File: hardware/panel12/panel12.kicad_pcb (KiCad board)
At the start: 2 copper layers, 99 x 92 mm, 300 parts, among them J1 Conn_01x02_Male, J2 Conn_01x08_Male, J3 Conn_01x02, J5 Conn_01x02_Male, J6 Conn_01x02_Male, J7 Conn_01x02_Male, U1 A7105-MODULE, U2 AIC1734-33GUTR, U3 ATtiny1617-M, U5 DRV8837DSGR, U6 DRV8837DSGR, U7 DRV8837DSGR

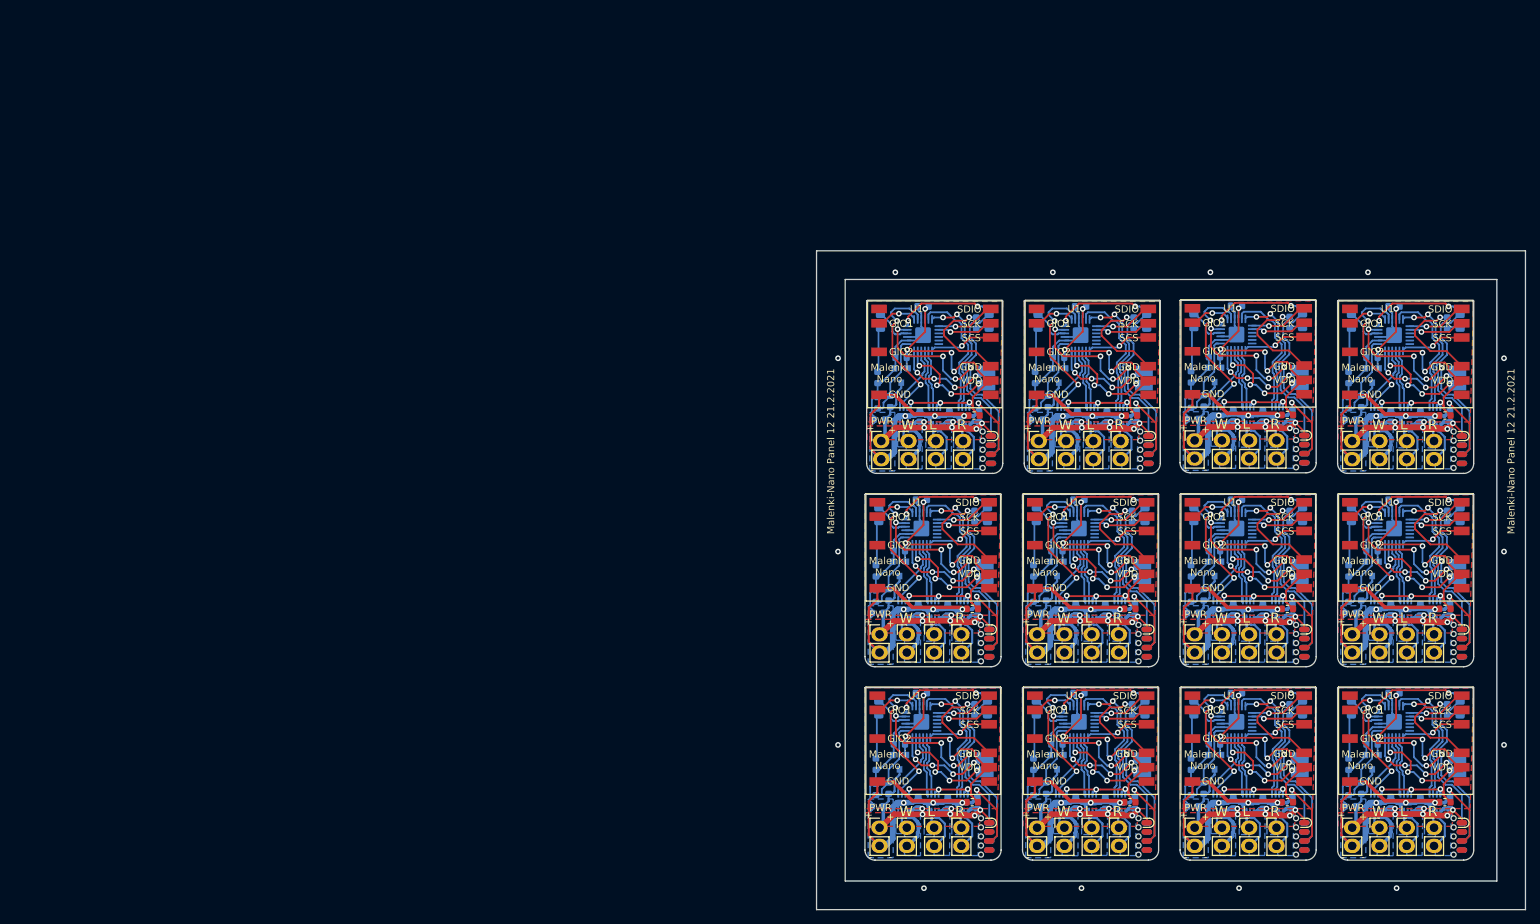
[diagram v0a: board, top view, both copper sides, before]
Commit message: Panel of 12 boards with the changes for tiny817
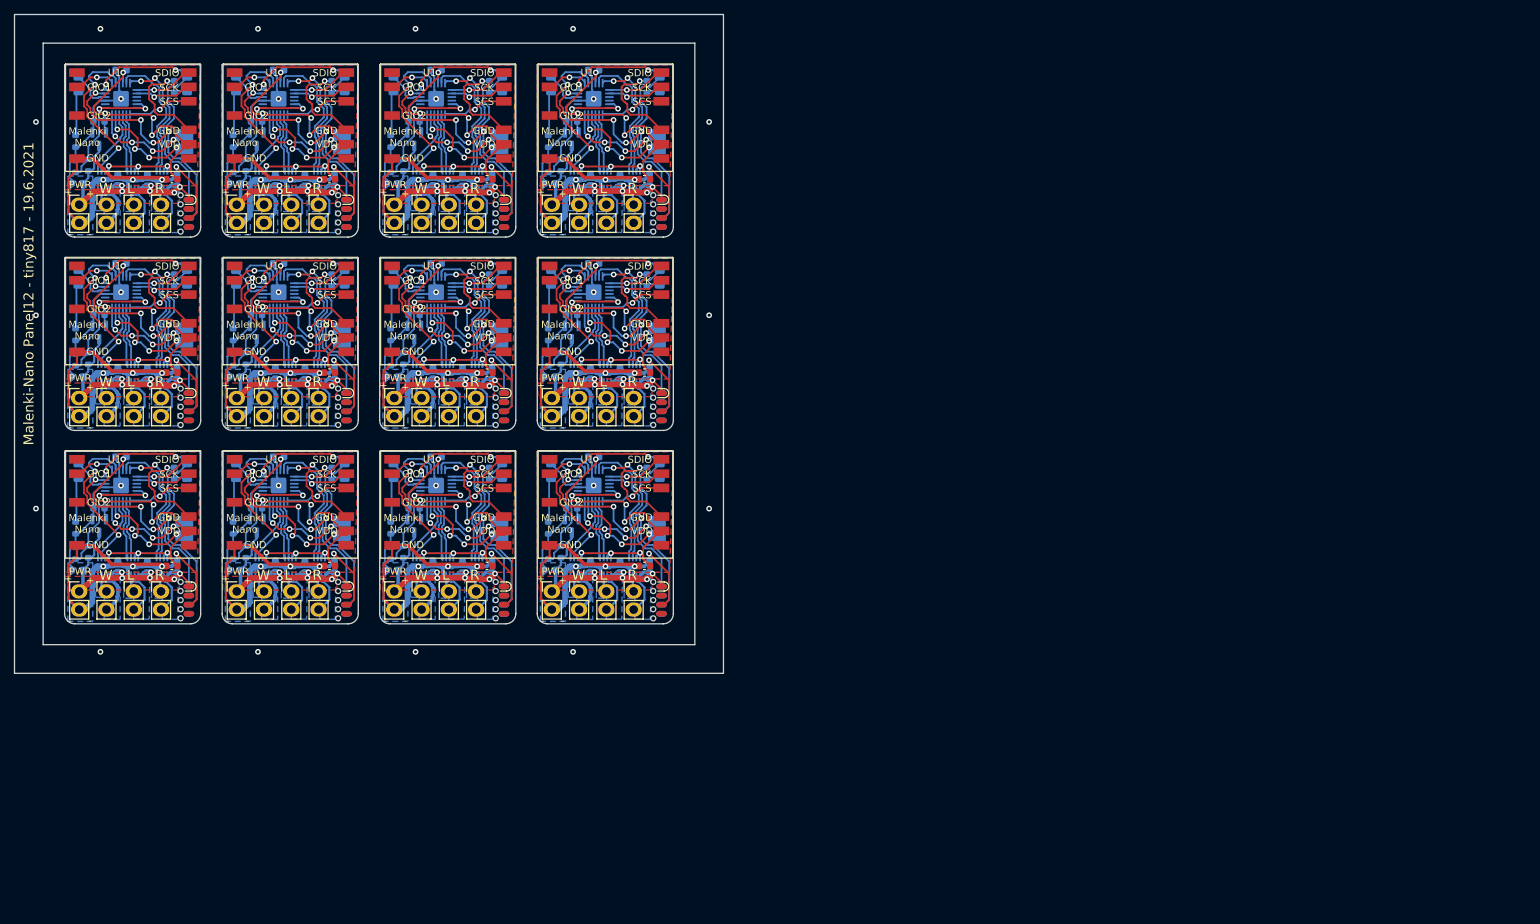
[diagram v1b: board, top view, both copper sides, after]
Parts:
- removed the C1 at (172.0, 96.0)
- removed the C1 at (193.8, 150.0)
- removed the C1 at (215.8, 150.0)
- removed the C1 at (215.8, 123.0)
- removed the C1 at (171.8, 123.0)
- removed the C1 at (171.8, 150.0)
- removed the C1 at (150.0, 96.0)
- removed the C1 at (193.8, 95.9)
- removed the C1 at (149.8, 150.0)
- removed the C1 at (193.8, 123.0)
- removed the C1 at (215.8, 96.0)
- removed the C1 at (149.8, 123.0)
- removed the C2 at (180.5, 123.6)
- removed the C2 at (202.5, 150.6)
- removed the C2 at (158.5, 150.6)
- removed the C2 at (180.5, 96.5)
- removed the C2 at (180.5, 150.6)
- removed the C2 at (202.5, 96.6)
- removed the C2 at (136.5, 150.6)
- removed the C2 at (158.8, 96.6)
- removed the C2 at (158.5, 123.6)
- removed the C2 at (136.8, 96.6)
- removed the C2 at (202.5, 123.6)
- removed the C2 at (136.5, 123.6)
- removed the C3 at (183.6, 114.9)
- removed the C3 at (205.6, 114.9)
- removed the C3 at (205.6, 87.9)
- removed the C3 at (139.8, 87.9)
- removed the C3 at (139.6, 114.9)
- removed the C3 at (161.6, 114.9)
- removed the C3 at (183.6, 87.8)
- removed the C3 at (205.6, 141.9)
- removed the C3 at (139.6, 141.9)
- removed the C3 at (183.6, 141.9)
- removed the C3 at (161.8, 87.9)
- removed the C3 at (161.6, 141.9)
- removed the C4 at (164.9, 80.8)
- removed the C4 at (208.6, 107.8)
- removed the C4 at (208.6, 80.8)
- removed the C4 at (164.6, 134.8)
- removed the C4 at (186.6, 107.8)
- removed the C4 at (142.6, 134.8)
- removed the C4 at (164.6, 107.8)
- removed the C4 at (142.9, 80.8)
- removed the C4 at (186.6, 80.7)
- removed the C4 at (208.6, 134.8)
- removed the C4 at (186.6, 134.8)
- removed the C4 at (142.6, 107.8)
- removed the C5 at (186.2, 96.0)
- removed the C5 at (142.4, 96.1)
- removed the C5 at (186.2, 123.1)
- removed the C5 at (186.2, 150.1)
- removed the C5 at (142.2, 123.1)
- removed the C5 at (208.2, 123.1)
- removed the C5 at (164.2, 150.1)
- removed the C5 at (164.2, 123.1)
- removed the C5 at (142.2, 150.1)
- removed the C5 at (208.2, 150.1)
- removed the C5 at (164.4, 96.1)
- removed the C5 at (208.2, 96.1)
- removed the C6 at (146.3, 150.1)
- removed the C6 at (212.3, 150.1)
- removed the C6 at (212.3, 123.1)
- removed the C6 at (190.3, 150.1)
- removed the C6 at (212.3, 96.1)
- removed the C6 at (190.3, 96.0)
- removed the C6 at (168.3, 123.1)
- removed the C6 at (168.3, 150.1)
- removed the C6 at (146.6, 96.1)
- removed the C6 at (168.6, 96.1)
- removed the C6 at (146.3, 123.1)
- removed the C6 at (190.3, 123.1)
- removed the C7 at (172.7, 96.1)
- removed the C7 at (172.4, 123.1)
- removed the C7 at (172.4, 150.1)
- removed the C7 at (216.4, 96.1)
- removed the C7 at (150.4, 123.1)
- removed the C7 at (216.4, 150.1)
- removed the C7 at (194.4, 96.0)
- removed the C7 at (150.7, 96.1)
- removed the C7 at (194.4, 150.1)
- removed the C7 at (194.4, 123.1)
- removed the C7 at (216.4, 123.1)
- removed the C7 at (150.4, 150.1)
- removed the D1 at (202.7, 109.7)
- removed the D1 at (202.7, 136.7)
- removed the D1 at (158.7, 109.7)
- removed the D1 at (136.7, 136.7)
- removed the D1 at (180.7, 109.7)
- removed the D1 at (158.9, 82.7)
- removed the D1 at (202.7, 82.7)
- removed the D1 at (180.7, 136.7)
- removed the D1 at (136.9, 82.7)
- removed the D1 at (158.7, 136.7)
- removed the D1 at (180.7, 82.6)
- removed the D1 at (136.7, 109.7)
- removed the D2 at (173.9, 136.7)
- removed the D2 at (195.9, 82.6)
- removed the D2 at (151.9, 136.7)
- removed the D2 at (217.9, 82.7)
- removed the D2 at (217.9, 109.7)
- removed the D2 at (152.1, 82.7)
- removed the D2 at (174.1, 82.7)
- removed the D2 at (173.9, 109.7)
- removed the D2 at (195.9, 136.7)
- removed the D2 at (195.9, 109.7)
- removed the D2 at (151.9, 109.7)
- removed the D2 at (217.9, 136.7)
- removed the J1 at (202.8, 153.6)
- removed the J1 at (159.0, 99.6)
- removed the J1 at (136.8, 153.6)
- removed the J1 at (202.8, 126.6)
- removed the J1 at (202.8, 99.6)
- removed the J1 at (180.8, 153.6)
- removed the J1 at (158.8, 126.6)
- removed the J1 at (180.8, 99.5)
- removed the J1 at (137.0, 99.6)
- removed the J1 at (180.8, 126.6)
- removed the J1 at (158.8, 153.6)
- removed the J1 at (136.8, 126.6)
- removed the J2 at (218.9, 154.8)
- removed the J2 at (152.9, 154.8)
- removed the J2 at (174.9, 154.8)
- removed the J2 at (174.9, 127.8)
- removed the J2 at (218.9, 127.8)
- removed the J2 at (218.9, 100.8)
- removed the J2 at (196.9, 154.8)
- removed the J2 at (175.1, 100.8)
- removed the J2 at (152.9, 127.8)
- removed the J2 at (196.9, 100.7)
- removed the J2 at (153.1, 100.8)
- removed the J2 at (196.9, 127.8)
- removed the J3 at (173.5, 144.8)
- removed the J3 at (151.5, 117.8)
- removed the J3 at (173.5, 117.8)
- removed the J3 at (217.5, 144.8)
- removed the J3 at (195.5, 117.8)
- removed the J3 at (151.5, 144.8)
- removed the J3 at (195.5, 144.8)
- removed the J3 at (217.5, 90.8)
- removed the J3 at (173.7, 90.8)
- removed the J3 at (151.7, 90.8)
- removed the J3 at (195.5, 90.7)
- removed the J3 at (217.5, 117.8)
- removed the J5 at (162.6, 153.6)
- removed the J5 at (206.6, 153.6)
- removed the J5 at (162.8, 99.6)
- removed the J5 at (140.8, 99.6)
- removed the J5 at (206.6, 99.6)
- removed the J5 at (184.6, 126.6)
- removed the J5 at (184.6, 99.5)
- removed the J5 at (206.6, 126.6)
- removed the J5 at (184.6, 153.6)
- removed the J5 at (162.6, 126.6)
- removed the J5 at (140.6, 126.6)
- removed the J5 at (140.6, 153.6)
- removed the J6 at (188.4, 99.5)
- removed the J6 at (166.7, 99.6)
- removed the J6 at (144.4, 153.6)
- removed the J6 at (210.4, 153.6)
- removed the J6 at (188.4, 153.6)
- removed the J6 at (210.4, 126.6)
- removed the J6 at (144.4, 126.6)
- removed the J6 at (166.4, 153.6)
- removed the J6 at (210.4, 99.6)
- removed the J6 at (188.4, 126.6)
- removed the J6 at (144.7, 99.6)
- removed the J6 at (166.4, 126.6)
- removed the J7 at (214.2, 126.6)
- removed the J7 at (170.2, 153.6)
- removed the J7 at (192.2, 153.6)
- removed the J7 at (170.2, 126.6)
- removed the J7 at (148.2, 126.6)
- removed the J7 at (214.2, 99.6)
- removed the J7 at (192.2, 126.6)
- removed the J7 at (170.5, 99.6)
- removed the J7 at (148.5, 99.6)
- removed the J7 at (214.2, 153.6)
- removed the J7 at (148.2, 153.6)
- removed the J7 at (192.2, 99.5)
- removed the R1 at (202.3, 144.7)
- removed the R1 at (158.3, 144.7)
- removed the R1 at (180.3, 144.7)
- removed the R1 at (158.5, 90.7)
- removed the R1 at (180.3, 90.6)
- removed the R1 at (136.3, 144.7)
- removed the R1 at (158.3, 117.7)
- removed the R1 at (136.3, 117.7)
- removed the R1 at (180.3, 117.7)
- removed the R1 at (202.3, 117.7)
- removed the R1 at (202.3, 90.7)
- removed the R1 at (136.5, 90.7)
- removed the R2 at (194.1, 137.1)
- removed the R2 at (150.1, 110.1)
- removed the R2 at (172.1, 110.1)
- removed the R2 at (172.1, 137.1)
- removed the R2 at (172.3, 83.1)
- removed the R2 at (216.1, 83.1)
- removed the R2 at (194.1, 83.0)
- removed the R2 at (150.3, 83.1)
- removed the R2 at (216.1, 137.1)
- removed the R2 at (150.1, 137.1)
- removed the R2 at (194.1, 110.1)
- removed the R2 at (216.1, 110.1)
- removed the R3 at (138.1, 121.0)
- removed the R3 at (182.1, 121.0)
- removed the R3 at (204.1, 148.0)
- removed the R3 at (138.3, 94.0)
- removed the R3 at (138.1, 148.0)
- removed the R3 at (160.3, 94.0)
- removed the R3 at (182.1, 148.0)
- removed the R3 at (160.1, 121.0)
- removed the R3 at (204.1, 121.0)
- removed the R3 at (182.1, 93.9)
- removed the R3 at (204.1, 94.0)
- removed the R3 at (160.1, 148.0)
- removed the R4 at (180.3, 121.2)
- removed the R4 at (158.3, 121.2)
- removed the R4 at (158.3, 148.2)
- removed the R4 at (180.3, 148.2)
- removed the R4 at (136.3, 121.2)
- removed the R4 at (180.3, 94.1)
- removed the R4 at (202.3, 148.2)
- removed the R4 at (158.5, 94.2)
- removed the R4 at (136.3, 148.2)
- removed the R4 at (202.3, 121.2)
- removed the R4 at (202.3, 94.2)
- removed the R4 at (136.5, 94.2)
- removed the U1 at (210.3, 141.1)
- removed the U1 at (188.3, 87.0)
- removed the U1 at (166.5, 87.1)
- removed the U1 at (144.3, 141.1)
- removed the U1 at (166.3, 114.1)
- removed the U1 at (166.3, 141.1)
- removed the U1 at (188.3, 114.1)
- removed the U1 at (188.3, 141.1)
- removed the U1 at (210.3, 87.1)
- removed the U1 at (144.5, 87.1)
- removed the U1 at (210.3, 114.1)
- removed the U1 at (144.3, 114.1)
- removed the U2 at (161.6, 117.4)
- removed the U2 at (139.6, 117.4)
- removed the U2 at (139.6, 144.4)
- removed the U2 at (205.6, 117.4)
- removed the U2 at (183.6, 90.3)
- removed the U2 at (161.6, 144.4)
- removed the U2 at (139.8, 90.4)
- removed the U2 at (161.8, 90.4)
- removed the U2 at (183.6, 117.4)
- removed the U2 at (205.6, 90.4)
- removed the U2 at (183.6, 144.4)
- removed the U2 at (205.6, 144.4)
- removed the U3 at (142.6, 138.8)
- removed the U3 at (186.6, 111.8)
- removed the U3 at (164.6, 138.8)
- removed the U3 at (186.6, 138.8)
- removed the U3 at (164.9, 84.8)
- removed the U3 at (142.6, 111.8)
- removed the U3 at (208.6, 84.8)
- removed the U3 at (208.6, 138.8)
- removed the U3 at (208.6, 111.8)
- removed the U3 at (142.9, 84.8)
- removed the U3 at (186.6, 84.7)
- removed the U3 at (164.6, 111.8)
- removed the U5 at (140.2, 123.1)
- removed the U5 at (140.4, 96.1)
- removed the U5 at (140.2, 150.1)
- removed the U5 at (184.2, 123.1)
- removed the U5 at (184.2, 96.0)
- removed the U5 at (184.2, 150.1)
- removed the U5 at (162.2, 150.1)
- removed the U5 at (162.2, 123.1)
- removed the U5 at (206.2, 96.1)
- removed the U5 at (162.4, 96.1)
- removed the U5 at (206.2, 123.1)
- removed the U5 at (206.2, 150.1)
- removed the U6 at (188.3, 96.0)
- removed the U6 at (144.3, 150.1)
- removed the U6 at (144.5, 96.1)
- removed the U6 at (188.3, 123.1)
- removed the U6 at (188.3, 150.1)
- removed the U6 at (166.3, 123.1)
- removed the U6 at (166.3, 150.1)
- removed the U6 at (210.3, 96.1)
- removed the U6 at (144.3, 123.1)
- removed the U6 at (210.3, 123.1)
- removed the U6 at (166.5, 96.1)
- removed the U6 at (210.3, 150.1)
- removed the U7 at (170.6, 96.1)
- removed the U7 at (214.4, 123.1)
- removed the U7 at (170.4, 123.1)
- removed the U7 at (148.6, 96.1)
- removed the U7 at (170.4, 150.1)
- removed the U7 at (192.4, 96.0)
- removed the U7 at (192.4, 150.1)
- removed the U7 at (214.4, 96.1)
- removed the U7 at (148.4, 150.1)
- removed the U7 at (214.4, 150.1)
- removed the U7 at (148.4, 123.1)
- removed the U7 at (192.4, 123.1)
- added C1: 0.1uF, Capacitor_SMD:C_0603_1608Metric, F.Cu at (104.0, 90.0)
- added C1: 0.1uF, Capacitor_SMD:C_0603_1608Metric, F.Cu at (60.0, 90.0)
- added C1: 0.1uF, Capacitor_SMD:C_0603_1608Metric, F.Cu at (38.0, 63.0)
- added C1: 0.1uF, Capacitor_SMD:C_0603_1608Metric, F.Cu at (104.0, 63.0)
- added C1: 0.1uF, Capacitor_SMD:C_0603_1608Metric, F.Cu at (60.0, 63.0)
- added C1: 0.1uF, Capacitor_SMD:C_0603_1608Metric, F.Cu at (104.0, 117.0)
- added C1: 0.1uF, Capacitor_SMD:C_0603_1608Metric, F.Cu at (38.0, 117.0)
- added C1: 0.1uF, Capacitor_SMD:C_0603_1608Metric, F.Cu at (82.0, 117.0)
- added C1: 0.1uF, Capacitor_SMD:C_0603_1608Metric, F.Cu at (38.0, 90.0)
- added C1: 0.1uF, Capacitor_SMD:C_0603_1608Metric, F.Cu at (82.0, 63.0)
- added C1: 0.1uF, Capacitor_SMD:C_0603_1608Metric, F.Cu at (60.0, 117.0)
- added C1: 0.1uF, Capacitor_SMD:C_0603_1608Metric, F.Cu at (82.0, 90.0)
- added C2: 10uF, Capacitor_SMD:C_0603_1608Metric, B.Cu at (46.8, 117.6)
- added C2: 10uF, Capacitor_SMD:C_0603_1608Metric, B.Cu at (90.8, 90.6)
- added C2: 10uF, Capacitor_SMD:C_0603_1608Metric, B.Cu at (24.8, 63.6)
- added C2: 10uF, Capacitor_SMD:C_0603_1608Metric, B.Cu at (90.8, 63.6)
- added C2: 10uF, Capacitor_SMD:C_0603_1608Metric, B.Cu at (68.8, 90.6)
- added C2: 10uF, Capacitor_SMD:C_0603_1608Metric, B.Cu at (24.8, 117.6)
- added C2: 10uF, Capacitor_SMD:C_0603_1608Metric, B.Cu at (46.8, 90.6)
- added C2: 10uF, Capacitor_SMD:C_0603_1608Metric, B.Cu at (46.8, 63.6)
- added C2: 10uF, Capacitor_SMD:C_0603_1608Metric, B.Cu at (24.8, 90.6)
- added C2: 10uF, Capacitor_SMD:C_0603_1608Metric, B.Cu at (68.8, 63.6)
- added C2: 10uF, Capacitor_SMD:C_0603_1608Metric, B.Cu at (90.8, 117.6)
- added C2: 10uF, Capacitor_SMD:C_0603_1608Metric, B.Cu at (68.8, 117.6)
- added C3: 10uF, Capacitor_SMD:C_0603_1608Metric, B.Cu at (49.8, 108.9)
- added C3: 10uF, Capacitor_SMD:C_0603_1608Metric, B.Cu at (27.8, 108.9)
- added C3: 10uF, Capacitor_SMD:C_0603_1608Metric, B.Cu at (71.8, 81.9)
- added C3: 10uF, Capacitor_SMD:C_0603_1608Metric, B.Cu at (27.8, 81.9)
- added C3: 10uF, Capacitor_SMD:C_0603_1608Metric, B.Cu at (93.8, 81.9)
- added C3: 10uF, Capacitor_SMD:C_0603_1608Metric, B.Cu at (71.8, 54.9)
- added C3: 10uF, Capacitor_SMD:C_0603_1608Metric, B.Cu at (27.8, 54.9)
- added C3: 10uF, Capacitor_SMD:C_0603_1608Metric, B.Cu at (49.8, 81.9)
- added C3: 10uF, Capacitor_SMD:C_0603_1608Metric, B.Cu at (71.8, 108.9)
- added C3: 10uF, Capacitor_SMD:C_0603_1608Metric, B.Cu at (93.8, 108.9)
- added C3: 10uF, Capacitor_SMD:C_0603_1608Metric, B.Cu at (93.8, 54.9)
- added C3: 10uF, Capacitor_SMD:C_0603_1608Metric, B.Cu at (49.8, 54.9)
- added C4: 0.1uF, Capacitor_SMD:C_0603_1608Metric, B.Cu at (52.9, 101.8)
- added C4: 0.1uF, Capacitor_SMD:C_0603_1608Metric, B.Cu at (30.9, 74.8)
- added C4: 0.1uF, Capacitor_SMD:C_0603_1608Metric, B.Cu at (52.9, 47.8)
- added C4: 0.1uF, Capacitor_SMD:C_0603_1608Metric, B.Cu at (74.9, 47.8)
- added C4: 0.1uF, Capacitor_SMD:C_0603_1608Metric, B.Cu at (30.9, 47.8)
- added C4: 0.1uF, Capacitor_SMD:C_0603_1608Metric, B.Cu at (74.9, 101.8)
- added C4: 0.1uF, Capacitor_SMD:C_0603_1608Metric, B.Cu at (96.9, 47.8)
- added C4: 0.1uF, Capacitor_SMD:C_0603_1608Metric, B.Cu at (74.9, 74.8)
- added C4: 0.1uF, Capacitor_SMD:C_0603_1608Metric, B.Cu at (30.9, 101.8)
- added C4: 0.1uF, Capacitor_SMD:C_0603_1608Metric, B.Cu at (52.9, 74.8)
- added C4: 0.1uF, Capacitor_SMD:C_0603_1608Metric, B.Cu at (96.9, 101.8)
- added C4: 0.1uF, Capacitor_SMD:C_0603_1608Metric, B.Cu at (96.9, 74.8)
- added C5: 10uF, Capacitor_SMD:C_0603_1608Metric, B.Cu at (30.4, 90.1)
- added C5: 10uF, Capacitor_SMD:C_0603_1608Metric, B.Cu at (30.4, 117.1)
- added C5: 10uF, Capacitor_SMD:C_0603_1608Metric, B.Cu at (52.4, 63.1)
- added C5: 10uF, Capacitor_SMD:C_0603_1608Metric, B.Cu at (96.4, 90.1)
- added C5: 10uF, Capacitor_SMD:C_0603_1608Metric, B.Cu at (52.4, 90.1)
- added C5: 10uF, Capacitor_SMD:C_0603_1608Metric, B.Cu at (74.4, 90.1)
- added C5: 10uF, Capacitor_SMD:C_0603_1608Metric, B.Cu at (96.4, 117.1)
- added C5: 10uF, Capacitor_SMD:C_0603_1608Metric, B.Cu at (74.4, 63.1)
- added C5: 10uF, Capacitor_SMD:C_0603_1608Metric, B.Cu at (52.4, 117.1)
- added C5: 10uF, Capacitor_SMD:C_0603_1608Metric, B.Cu at (96.4, 63.1)
- added C5: 10uF, Capacitor_SMD:C_0603_1608Metric, B.Cu at (30.4, 63.1)
- added C5: 10uF, Capacitor_SMD:C_0603_1608Metric, B.Cu at (74.4, 117.1)
- added C6: 10uF, Capacitor_SMD:C_0603_1608Metric, B.Cu at (56.6, 63.1)
- added C6: 10uF, Capacitor_SMD:C_0603_1608Metric, B.Cu at (100.6, 90.1)
- added C6: 10uF, Capacitor_SMD:C_0603_1608Metric, B.Cu at (56.6, 90.1)
- added C6: 10uF, Capacitor_SMD:C_0603_1608Metric, B.Cu at (100.6, 63.1)
- added C6: 10uF, Capacitor_SMD:C_0603_1608Metric, B.Cu at (56.6, 117.1)
- added C6: 10uF, Capacitor_SMD:C_0603_1608Metric, B.Cu at (34.6, 63.1)
- added C6: 10uF, Capacitor_SMD:C_0603_1608Metric, B.Cu at (34.6, 90.1)
- added C6: 10uF, Capacitor_SMD:C_0603_1608Metric, B.Cu at (78.6, 90.1)
- added C6: 10uF, Capacitor_SMD:C_0603_1608Metric, B.Cu at (78.6, 63.1)
- added C6: 10uF, Capacitor_SMD:C_0603_1608Metric, B.Cu at (78.6, 117.1)
- added C6: 10uF, Capacitor_SMD:C_0603_1608Metric, B.Cu at (34.6, 117.1)
- added C6: 10uF, Capacitor_SMD:C_0603_1608Metric, B.Cu at (100.6, 117.1)
- added C7: 10uF, Capacitor_SMD:C_0603_1608Metric, B.Cu at (60.7, 63.1)
- added C7: 10uF, Capacitor_SMD:C_0603_1608Metric, B.Cu at (38.7, 117.1)
- added C7: 10uF, Capacitor_SMD:C_0603_1608Metric, B.Cu at (60.7, 90.1)
- added C7: 10uF, Capacitor_SMD:C_0603_1608Metric, B.Cu at (38.7, 90.1)
- added C7: 10uF, Capacitor_SMD:C_0603_1608Metric, B.Cu at (38.7, 63.1)
- added C7: 10uF, Capacitor_SMD:C_0603_1608Metric, B.Cu at (104.7, 90.1)
- added C7: 10uF, Capacitor_SMD:C_0603_1608Metric, B.Cu at (82.7, 117.1)
- added C7: 10uF, Capacitor_SMD:C_0603_1608Metric, B.Cu at (82.7, 63.1)
- added C7: 10uF, Capacitor_SMD:C_0603_1608Metric, B.Cu at (82.7, 90.1)
- added C7: 10uF, Capacitor_SMD:C_0603_1608Metric, B.Cu at (104.7, 63.1)
- added C7: 10uF, Capacitor_SMD:C_0603_1608Metric, B.Cu at (60.7, 117.1)
- added C7: 10uF, Capacitor_SMD:C_0603_1608Metric, B.Cu at (104.7, 117.1)
- added D1: LED Blue, LED_SMD:LED_0805_2012Metric_Pad1.15x1.40mm_HandSolder, B.Cu at (90.9, 103.7)
- added D1: LED Blue, LED_SMD:LED_0805_2012Metric_Pad1.15x1.40mm_HandSolder, B.Cu at (24.9, 103.7)
- added D1: LED Blue, LED_SMD:LED_0805_2012Metric_Pad1.15x1.40mm_HandSolder, B.Cu at (90.9, 76.7)
- added D1: LED Blue, LED_SMD:LED_0805_2012Metric_Pad1.15x1.40mm_HandSolder, B.Cu at (46.9, 103.7)
- added D1: LED Blue, LED_SMD:LED_0805_2012Metric_Pad1.15x1.40mm_HandSolder, B.Cu at (24.9, 49.7)
- added D1: LED Blue, LED_SMD:LED_0805_2012Metric_Pad1.15x1.40mm_HandSolder, B.Cu at (68.9, 49.7)
- added D1: LED Blue, LED_SMD:LED_0805_2012Metric_Pad1.15x1.40mm_HandSolder, B.Cu at (24.9, 76.7)
- added D1: LED Blue, LED_SMD:LED_0805_2012Metric_Pad1.15x1.40mm_HandSolder, B.Cu at (46.9, 76.7)
- added D1: LED Blue, LED_SMD:LED_0805_2012Metric_Pad1.15x1.40mm_HandSolder, B.Cu at (46.9, 49.7)
- added D1: LED Blue, LED_SMD:LED_0805_2012Metric_Pad1.15x1.40mm_HandSolder, B.Cu at (68.9, 103.7)
- added D1: LED Blue, LED_SMD:LED_0805_2012Metric_Pad1.15x1.40mm_HandSolder, B.Cu at (90.9, 49.7)
- added D1: LED Blue, LED_SMD:LED_0805_2012Metric_Pad1.15x1.40mm_HandSolder, B.Cu at (68.9, 76.7)
- added D2: LED Red, LED_SMD:LED_0805_2012Metric_Pad1.15x1.40mm_HandSolder, B.Cu at (62.1, 49.7)
- added D2: LED Red, LED_SMD:LED_0805_2012Metric_Pad1.15x1.40mm_HandSolder, B.Cu at (40.1, 76.7)
- added D2: LED Red, LED_SMD:LED_0805_2012Metric_Pad1.15x1.40mm_HandSolder, B.Cu at (84.1, 76.7)
- added D2: LED Red, LED_SMD:LED_0805_2012Metric_Pad1.15x1.40mm_HandSolder, B.Cu at (84.1, 103.7)
- added D2: LED Red, LED_SMD:LED_0805_2012Metric_Pad1.15x1.40mm_HandSolder, B.Cu at (106.1, 49.7)
- added D2: LED Red, LED_SMD:LED_0805_2012Metric_Pad1.15x1.40mm_HandSolder, B.Cu at (84.1, 49.7)
- added D2: LED Red, LED_SMD:LED_0805_2012Metric_Pad1.15x1.40mm_HandSolder, B.Cu at (106.1, 103.7)
- added D2: LED Red, LED_SMD:LED_0805_2012Metric_Pad1.15x1.40mm_HandSolder, B.Cu at (40.1, 49.7)
- added D2: LED Red, LED_SMD:LED_0805_2012Metric_Pad1.15x1.40mm_HandSolder, B.Cu at (62.1, 76.7)
- added D2: LED Red, LED_SMD:LED_0805_2012Metric_Pad1.15x1.40mm_HandSolder, B.Cu at (62.1, 103.7)
- added D2: LED Red, LED_SMD:LED_0805_2012Metric_Pad1.15x1.40mm_HandSolder, B.Cu at (106.1, 76.7)
- added D2: LED Red, LED_SMD:LED_0805_2012Metric_Pad1.15x1.40mm_HandSolder, B.Cu at (40.1, 103.7)
- added J1: Conn_01x02_Male, malenki-nano:PinHeader_1x02_P2.54mm_BIG1, F.Cu at (25.0, 93.6)
- added J1: Conn_01x02_Male, malenki-nano:PinHeader_1x02_P2.54mm_BIG1, F.Cu at (69.0, 66.6)
- added J1: Conn_01x02_Male, malenki-nano:PinHeader_1x02_P2.54mm_BIG1, F.Cu at (25.0, 66.6)
- added J1: Conn_01x02_Male, malenki-nano:PinHeader_1x02_P2.54mm_BIG1, F.Cu at (47.0, 120.6)
- added J1: Conn_01x02_Male, malenki-nano:PinHeader_1x02_P2.54mm_BIG1, F.Cu at (69.0, 120.6)
- added J1: Conn_01x02_Male, malenki-nano:PinHeader_1x02_P2.54mm_BIG1, F.Cu at (47.0, 66.6)
- added J1: Conn_01x02_Male, malenki-nano:PinHeader_1x02_P2.54mm_BIG1, F.Cu at (47.0, 93.6)
- added J1: Conn_01x02_Male, malenki-nano:PinHeader_1x02_P2.54mm_BIG1, F.Cu at (91.0, 93.6)
- added J1: Conn_01x02_Male, malenki-nano:PinHeader_1x02_P2.54mm_BIG1, F.Cu at (91.0, 120.6)
- added J1: Conn_01x02_Male, malenki-nano:PinHeader_1x02_P2.54mm_BIG1, F.Cu at (91.0, 66.6)
- added J1: Conn_01x02_Male, malenki-nano:PinHeader_1x02_P2.54mm_BIG1, F.Cu at (25.0, 120.6)
- added J1: Conn_01x02_Male, malenki-nano:PinHeader_1x02_P2.54mm_BIG1, F.Cu at (69.0, 93.6)
- added J2: Conn_01x08_Male, malenki-nano:SOIC_clipProgSmall, F.Cu at (107.1, 121.8)
- added J2: Conn_01x08_Male, malenki-nano:SOIC_clipProgSmall, F.Cu at (107.1, 94.8)
- added J2: Conn_01x08_Male, malenki-nano:SOIC_clipProgSmall, F.Cu at (41.1, 121.8)
- added J2: Conn_01x08_Male, malenki-nano:SOIC_clipProgSmall, F.Cu at (63.1, 94.8)
- added J2: Conn_01x08_Male, malenki-nano:SOIC_clipProgSmall, F.Cu at (85.1, 121.8)
- added J2: Conn_01x08_Male, malenki-nano:SOIC_clipProgSmall, F.Cu at (107.1, 67.8)
- added J2: Conn_01x08_Male, malenki-nano:SOIC_clipProgSmall, F.Cu at (41.1, 67.8)
- added J2: Conn_01x08_Male, malenki-nano:SOIC_clipProgSmall, F.Cu at (85.1, 94.8)
- added J2: Conn_01x08_Male, malenki-nano:SOIC_clipProgSmall, F.Cu at (63.1, 67.8)
- added J2: Conn_01x08_Male, malenki-nano:SOIC_clipProgSmall, F.Cu at (63.1, 121.8)
- added J2: Conn_01x08_Male, malenki-nano:SOIC_clipProgSmall, F.Cu at (41.1, 94.8)
- added J2: Conn_01x08_Male, malenki-nano:SOIC_clipProgSmall, F.Cu at (85.1, 67.8)
- added J3: Conn_01x02, malenki-nano:wirepad_2, B.Cu at (61.7, 84.8)
- added J3: Conn_01x02, malenki-nano:wirepad_2, B.Cu at (83.7, 111.8)
- added J3: Conn_01x02, malenki-nano:wirepad_2, B.Cu at (39.7, 57.8)
- added J3: Conn_01x02, malenki-nano:wirepad_2, B.Cu at (39.7, 84.8)
- added J3: Conn_01x02, malenki-nano:wirepad_2, B.Cu at (61.7, 57.8)
- added J3: Conn_01x02, malenki-nano:wirepad_2, B.Cu at (61.7, 111.8)
- added J3: Conn_01x02, malenki-nano:wirepad_2, B.Cu at (105.7, 84.8)
- added J3: Conn_01x02, malenki-nano:wirepad_2, B.Cu at (83.7, 57.8)
- added J3: Conn_01x02, malenki-nano:wirepad_2, B.Cu at (83.7, 84.8)
- added J3: Conn_01x02, malenki-nano:wirepad_2, B.Cu at (105.7, 111.8)
- added J3: Conn_01x02, malenki-nano:wirepad_2, B.Cu at (39.7, 111.8)
- added J3: Conn_01x02, malenki-nano:wirepad_2, B.Cu at (105.7, 57.8)
- added J5: Conn_01x02_Male, malenki-nano:PinHeader_1x02_P2.54mm_BIG1, F.Cu at (50.8, 93.6)
- added J5: Conn_01x02_Male, malenki-nano:PinHeader_1x02_P2.54mm_BIG1, F.Cu at (50.8, 120.6)
- added J5: Conn_01x02_Male, malenki-nano:PinHeader_1x02_P2.54mm_BIG1, F.Cu at (72.8, 120.6)
- added J5: Conn_01x02_Male, malenki-nano:PinHeader_1x02_P2.54mm_BIG1, F.Cu at (50.8, 66.6)
- added J5: Conn_01x02_Male, malenki-nano:PinHeader_1x02_P2.54mm_BIG1, F.Cu at (94.8, 120.6)
- added J5: Conn_01x02_Male, malenki-nano:PinHeader_1x02_P2.54mm_BIG1, F.Cu at (28.8, 66.6)
- added J5: Conn_01x02_Male, malenki-nano:PinHeader_1x02_P2.54mm_BIG1, F.Cu at (72.8, 93.6)
- added J5: Conn_01x02_Male, malenki-nano:PinHeader_1x02_P2.54mm_BIG1, F.Cu at (28.8, 120.6)
- added J5: Conn_01x02_Male, malenki-nano:PinHeader_1x02_P2.54mm_BIG1, F.Cu at (28.8, 93.6)
- added J5: Conn_01x02_Male, malenki-nano:PinHeader_1x02_P2.54mm_BIG1, F.Cu at (72.8, 66.6)
- added J5: Conn_01x02_Male, malenki-nano:PinHeader_1x02_P2.54mm_BIG1, F.Cu at (94.8, 66.6)
- added J5: Conn_01x02_Male, malenki-nano:PinHeader_1x02_P2.54mm_BIG1, F.Cu at (94.8, 93.6)
- added J6: Conn_01x02_Male, malenki-nano:PinHeader_1x02_P2.54mm_BIG1, F.Cu at (76.7, 66.6)
- added J6: Conn_01x02_Male, malenki-nano:PinHeader_1x02_P2.54mm_BIG1, F.Cu at (32.7, 66.6)
- added J6: Conn_01x02_Male, malenki-nano:PinHeader_1x02_P2.54mm_BIG1, F.Cu at (32.7, 120.6)
- added J6: Conn_01x02_Male, malenki-nano:PinHeader_1x02_P2.54mm_BIG1, F.Cu at (54.7, 120.6)
- added J6: Conn_01x02_Male, malenki-nano:PinHeader_1x02_P2.54mm_BIG1, F.Cu at (54.7, 66.6)
- added J6: Conn_01x02_Male, malenki-nano:PinHeader_1x02_P2.54mm_BIG1, F.Cu at (98.7, 66.6)
- added J6: Conn_01x02_Male, malenki-nano:PinHeader_1x02_P2.54mm_BIG1, F.Cu at (32.7, 93.6)
- added J6: Conn_01x02_Male, malenki-nano:PinHeader_1x02_P2.54mm_BIG1, F.Cu at (98.7, 120.6)
- added J6: Conn_01x02_Male, malenki-nano:PinHeader_1x02_P2.54mm_BIG1, F.Cu at (76.7, 120.6)
- added J6: Conn_01x02_Male, malenki-nano:PinHeader_1x02_P2.54mm_BIG1, F.Cu at (98.7, 93.6)
- added J6: Conn_01x02_Male, malenki-nano:PinHeader_1x02_P2.54mm_BIG1, F.Cu at (54.7, 93.6)
- added J6: Conn_01x02_Male, malenki-nano:PinHeader_1x02_P2.54mm_BIG1, F.Cu at (76.7, 93.6)
- added J7: Conn_01x02_Male, malenki-nano:PinHeader_1x02_P2.54mm_BIG1, F.Cu at (58.5, 66.6)
- added J7: Conn_01x02_Male, malenki-nano:PinHeader_1x02_P2.54mm_BIG1, F.Cu at (58.5, 120.6)
- added J7: Conn_01x02_Male, malenki-nano:PinHeader_1x02_P2.54mm_BIG1, F.Cu at (102.5, 120.6)
- added J7: Conn_01x02_Male, malenki-nano:PinHeader_1x02_P2.54mm_BIG1, F.Cu at (80.5, 120.6)
- added J7: Conn_01x02_Male, malenki-nano:PinHeader_1x02_P2.54mm_BIG1, F.Cu at (80.5, 93.6)
- added J7: Conn_01x02_Male, malenki-nano:PinHeader_1x02_P2.54mm_BIG1, F.Cu at (102.5, 66.6)
- added J7: Conn_01x02_Male, malenki-nano:PinHeader_1x02_P2.54mm_BIG1, F.Cu at (80.5, 66.6)
- added J7: Conn_01x02_Male, malenki-nano:PinHeader_1x02_P2.54mm_BIG1, F.Cu at (36.5, 93.6)
- added J7: Conn_01x02_Male, malenki-nano:PinHeader_1x02_P2.54mm_BIG1, F.Cu at (36.5, 120.6)
- added J7: Conn_01x02_Male, malenki-nano:PinHeader_1x02_P2.54mm_BIG1, F.Cu at (58.5, 93.6)
- added J7: Conn_01x02_Male, malenki-nano:PinHeader_1x02_P2.54mm_BIG1, F.Cu at (102.5, 93.6)
- added J7: Conn_01x02_Male, malenki-nano:PinHeader_1x02_P2.54mm_BIG1, F.Cu at (36.5, 66.6)
- added R1: 220R, Resistor_SMD:R_0603_1608Metric, B.Cu at (68.5, 84.7)
- added R1: 220R, Resistor_SMD:R_0603_1608Metric, B.Cu at (46.5, 57.7)
- added R1: 220R, Resistor_SMD:R_0603_1608Metric, B.Cu at (90.5, 57.7)
- added R1: 220R, Resistor_SMD:R_0603_1608Metric, B.Cu at (68.5, 111.7)
- added R1: 220R, Resistor_SMD:R_0603_1608Metric, B.Cu at (24.5, 111.7)
- added R1: 220R, Resistor_SMD:R_0603_1608Metric, B.Cu at (46.5, 111.7)
- added R1: 220R, Resistor_SMD:R_0603_1608Metric, B.Cu at (24.5, 84.7)
- added R1: 220R, Resistor_SMD:R_0603_1608Metric, B.Cu at (24.5, 57.7)
- added R1: 220R, Resistor_SMD:R_0603_1608Metric, B.Cu at (68.5, 57.7)
- added R1: 220R, Resistor_SMD:R_0603_1608Metric, B.Cu at (90.5, 84.7)
- added R1: 220R, Resistor_SMD:R_0603_1608Metric, B.Cu at (90.5, 111.7)
- added R1: 220R, Resistor_SMD:R_0603_1608Metric, B.Cu at (46.5, 84.7)
- added R2: 220R, Resistor_SMD:R_0603_1608Metric, B.Cu at (82.3, 77.1)
- added R2: 220R, Resistor_SMD:R_0603_1608Metric, B.Cu at (38.3, 77.1)
- added R2: 220R, Resistor_SMD:R_0603_1608Metric, B.Cu at (104.3, 50.1)
- added R2: 220R, Resistor_SMD:R_0603_1608Metric, B.Cu at (60.3, 104.1)
- added R2: 220R, Resistor_SMD:R_0603_1608Metric, B.Cu at (60.3, 50.1)
- added R2: 220R, Resistor_SMD:R_0603_1608Metric, B.Cu at (82.3, 104.1)
- added R2: 220R, Resistor_SMD:R_0603_1608Metric, B.Cu at (82.3, 50.1)
- added R2: 220R, Resistor_SMD:R_0603_1608Metric, B.Cu at (60.3, 77.1)
- added R2: 220R, Resistor_SMD:R_0603_1608Metric, B.Cu at (38.3, 104.1)
- added R2: 220R, Resistor_SMD:R_0603_1608Metric, B.Cu at (38.3, 50.1)
- added R2: 220R, Resistor_SMD:R_0603_1608Metric, B.Cu at (104.3, 104.1)
- added R2: 220R, Resistor_SMD:R_0603_1608Metric, B.Cu at (104.3, 77.1)
- added R3: 33k, Resistor_SMD:R_0603_1608Metric, B.Cu at (92.3, 61.0)
- added R3: 33k, Resistor_SMD:R_0603_1608Metric, B.Cu at (48.3, 61.0)
- added R3: 33k, Resistor_SMD:R_0603_1608Metric, B.Cu at (26.3, 61.0)
- added R3: 33k, Resistor_SMD:R_0603_1608Metric, B.Cu at (92.3, 115.0)
- added R3: 33k, Resistor_SMD:R_0603_1608Metric, B.Cu at (92.3, 88.0)
- added R3: 33k, Resistor_SMD:R_0603_1608Metric, B.Cu at (48.3, 88.0)
- added R3: 33k, Resistor_SMD:R_0603_1608Metric, B.Cu at (26.3, 88.0)
- added R3: 33k, Resistor_SMD:R_0603_1608Metric, B.Cu at (26.3, 115.0)
- added R3: 33k, Resistor_SMD:R_0603_1608Metric, B.Cu at (70.3, 88.0)
- added R3: 33k, Resistor_SMD:R_0603_1608Metric, B.Cu at (70.3, 61.0)
- added R3: 33k, Resistor_SMD:R_0603_1608Metric, B.Cu at (48.3, 115.0)
- added R3: 33k, Resistor_SMD:R_0603_1608Metric, B.Cu at (70.3, 115.0)
- added R4: 10k, Resistor_SMD:R_0603_1608Metric, B.Cu at (24.5, 115.2)
- added R4: 10k, Resistor_SMD:R_0603_1608Metric, B.Cu at (68.5, 115.2)
- added R4: 10k, Resistor_SMD:R_0603_1608Metric, B.Cu at (90.5, 61.2)
- added R4: 10k, Resistor_SMD:R_0603_1608Metric, B.Cu at (46.5, 115.2)
- added R4: 10k, Resistor_SMD:R_0603_1608Metric, B.Cu at (24.5, 61.2)
- added R4: 10k, Resistor_SMD:R_0603_1608Metric, B.Cu at (68.5, 61.2)
- added R4: 10k, Resistor_SMD:R_0603_1608Metric, B.Cu at (68.5, 88.2)
- added R4: 10k, Resistor_SMD:R_0603_1608Metric, B.Cu at (90.5, 88.2)
- added R4: 10k, Resistor_SMD:R_0603_1608Metric, B.Cu at (46.5, 61.2)
- added R4: 10k, Resistor_SMD:R_0603_1608Metric, B.Cu at (24.5, 88.2)
- added R4: 10k, Resistor_SMD:R_0603_1608Metric, B.Cu at (46.5, 88.2)
- added R4: 10k, Resistor_SMD:R_0603_1608Metric, B.Cu at (90.5, 115.2)
- added U1: A7105-MODULE, malenki-nano:A7105-module, F.Cu at (76.5, 108.1)
- added U1: A7105-MODULE, malenki-nano:A7105-module, F.Cu at (54.5, 54.1)
- added U1: A7105-MODULE, malenki-nano:A7105-module, F.Cu at (76.5, 54.1)
- added U1: A7105-MODULE, malenki-nano:A7105-module, F.Cu at (98.5, 54.1)
- added U1: A7105-MODULE, malenki-nano:A7105-module, F.Cu at (54.5, 81.1)
- added U1: A7105-MODULE, malenki-nano:A7105-module, F.Cu at (98.5, 108.1)
- added U1: A7105-MODULE, malenki-nano:A7105-module, F.Cu at (54.5, 108.1)
- added U1: A7105-MODULE, malenki-nano:A7105-module, F.Cu at (32.5, 54.1)
- added U1: A7105-MODULE, malenki-nano:A7105-module, F.Cu at (32.5, 108.1)
- added U1: A7105-MODULE, malenki-nano:A7105-module, F.Cu at (98.5, 81.1)
- added U1: A7105-MODULE, malenki-nano:A7105-module, F.Cu at (76.5, 81.1)
- added U1: A7105-MODULE, malenki-nano:A7105-module, F.Cu at (32.5, 81.1)
- added U2: AIC1734-33GUTR, Package_TO_SOT_SMD:SOT-23, B.Cu at (49.8, 84.4)
- added U2: AIC1734-33GUTR, Package_TO_SOT_SMD:SOT-23, B.Cu at (93.8, 84.4)
- added U2: AIC1734-33GUTR, Package_TO_SOT_SMD:SOT-23, B.Cu at (27.8, 84.4)
- added U2: AIC1734-33GUTR, Package_TO_SOT_SMD:SOT-23, B.Cu at (71.8, 111.4)
- added U2: AIC1734-33GUTR, Package_TO_SOT_SMD:SOT-23, B.Cu at (93.8, 57.4)
- added U2: AIC1734-33GUTR, Package_TO_SOT_SMD:SOT-23, B.Cu at (27.8, 57.4)
- added U2: AIC1734-33GUTR, Package_TO_SOT_SMD:SOT-23, B.Cu at (71.8, 57.4)
- added U2: AIC1734-33GUTR, Package_TO_SOT_SMD:SOT-23, B.Cu at (93.8, 111.4)
- added U2: AIC1734-33GUTR, Package_TO_SOT_SMD:SOT-23, B.Cu at (71.8, 84.4)
- added U2: AIC1734-33GUTR, Package_TO_SOT_SMD:SOT-23, B.Cu at (49.8, 111.4)
- added U2: AIC1734-33GUTR, Package_TO_SOT_SMD:SOT-23, B.Cu at (49.8, 57.4)
- added U2: AIC1734-33GUTR, Package_TO_SOT_SMD:SOT-23, B.Cu at (27.8, 111.4)
- added U3: ATtiny817-M, malenki-nano:qfn24-hand1, B.Cu at (96.9, 51.8)
- added U3: ATtiny817-M, malenki-nano:qfn24-hand1, B.Cu at (74.9, 105.8)
- added U3: ATtiny817-M, malenki-nano:qfn24-hand1, B.Cu at (30.9, 105.8)
- added U3: ATtiny817-M, malenki-nano:qfn24-hand1, B.Cu at (96.9, 78.8)
- added U3: ATtiny817-M, malenki-nano:qfn24-hand1, B.Cu at (30.9, 78.8)
- added U3: ATtiny817-M, malenki-nano:qfn24-hand1, B.Cu at (52.9, 105.8)
- added U3: ATtiny817-M, malenki-nano:qfn24-hand1, B.Cu at (52.9, 51.8)
- added U3: ATtiny817-M, malenki-nano:qfn24-hand1, B.Cu at (30.9, 51.8)
- added U3: ATtiny817-M, malenki-nano:qfn24-hand1, B.Cu at (74.9, 51.8)
- added U3: ATtiny817-M, malenki-nano:qfn24-hand1, B.Cu at (96.9, 105.8)
- added U3: ATtiny817-M, malenki-nano:qfn24-hand1, B.Cu at (74.9, 78.8)
- added U3: ATtiny817-M, malenki-nano:qfn24-hand1, B.Cu at (52.9, 78.8)
- added U5: DRV8837DSGR, malenki-nano:WSON-8-1EP_2x2mm_P0.5mm_HAND1, B.Cu at (28.4, 117.1)
- added U5: DRV8837DSGR, malenki-nano:WSON-8-1EP_2x2mm_P0.5mm_HAND1, B.Cu at (72.4, 117.1)
- added U5: DRV8837DSGR, malenki-nano:WSON-8-1EP_2x2mm_P0.5mm_HAND1, B.Cu at (28.4, 63.1)
- added U5: DRV8837DSGR, malenki-nano:WSON-8-1EP_2x2mm_P0.5mm_HAND1, B.Cu at (94.4, 90.1)
- added U5: DRV8837DSGR, malenki-nano:WSON-8-1EP_2x2mm_P0.5mm_HAND1, B.Cu at (72.4, 63.1)
- added U5: DRV8837DSGR, malenki-nano:WSON-8-1EP_2x2mm_P0.5mm_HAND1, B.Cu at (50.4, 63.1)
- added U5: DRV8837DSGR, malenki-nano:WSON-8-1EP_2x2mm_P0.5mm_HAND1, B.Cu at (94.4, 117.1)
- added U5: DRV8837DSGR, malenki-nano:WSON-8-1EP_2x2mm_P0.5mm_HAND1, B.Cu at (50.4, 117.1)
- added U5: DRV8837DSGR, malenki-nano:WSON-8-1EP_2x2mm_P0.5mm_HAND1, B.Cu at (94.4, 63.1)
- added U5: DRV8837DSGR, malenki-nano:WSON-8-1EP_2x2mm_P0.5mm_HAND1, B.Cu at (72.4, 90.1)
- added U5: DRV8837DSGR, malenki-nano:WSON-8-1EP_2x2mm_P0.5mm_HAND1, B.Cu at (28.4, 90.1)
- added U5: DRV8837DSGR, malenki-nano:WSON-8-1EP_2x2mm_P0.5mm_HAND1, B.Cu at (50.4, 90.1)
- added U6: DRV8837DSGR, malenki-nano:WSON-8-1EP_2x2mm_P0.5mm_HAND1, B.Cu at (32.5, 63.1)
- added U6: DRV8837DSGR, malenki-nano:WSON-8-1EP_2x2mm_P0.5mm_HAND1, B.Cu at (76.5, 117.1)
- added U6: DRV8837DSGR, malenki-nano:WSON-8-1EP_2x2mm_P0.5mm_HAND1, B.Cu at (76.5, 63.1)
- added U6: DRV8837DSGR, malenki-nano:WSON-8-1EP_2x2mm_P0.5mm_HAND1, B.Cu at (54.5, 63.1)
- added U6: DRV8837DSGR, malenki-nano:WSON-8-1EP_2x2mm_P0.5mm_HAND1, B.Cu at (98.5, 90.1)
- added U6: DRV8837DSGR, malenki-nano:WSON-8-1EP_2x2mm_P0.5mm_HAND1, B.Cu at (98.5, 63.1)
- added U6: DRV8837DSGR, malenki-nano:WSON-8-1EP_2x2mm_P0.5mm_HAND1, B.Cu at (98.5, 117.1)
- added U6: DRV8837DSGR, malenki-nano:WSON-8-1EP_2x2mm_P0.5mm_HAND1, B.Cu at (76.5, 90.1)
- added U6: DRV8837DSGR, malenki-nano:WSON-8-1EP_2x2mm_P0.5mm_HAND1, B.Cu at (54.5, 117.1)
- added U6: DRV8837DSGR, malenki-nano:WSON-8-1EP_2x2mm_P0.5mm_HAND1, B.Cu at (32.5, 90.1)
- added U6: DRV8837DSGR, malenki-nano:WSON-8-1EP_2x2mm_P0.5mm_HAND1, B.Cu at (32.5, 117.1)
- added U6: DRV8837DSGR, malenki-nano:WSON-8-1EP_2x2mm_P0.5mm_HAND1, B.Cu at (54.5, 90.1)
- added U7: DRV8837DSGR, malenki-nano:WSON-8-1EP_2x2mm_P0.5mm_HAND1, B.Cu at (58.6, 90.1)
- added U7: DRV8837DSGR, malenki-nano:WSON-8-1EP_2x2mm_P0.5mm_HAND1, B.Cu at (36.6, 117.1)
- added U7: DRV8837DSGR, malenki-nano:WSON-8-1EP_2x2mm_P0.5mm_HAND1, B.Cu at (80.6, 63.1)
- added U7: DRV8837DSGR, malenki-nano:WSON-8-1EP_2x2mm_P0.5mm_HAND1, B.Cu at (102.6, 90.1)
- added U7: DRV8837DSGR, malenki-nano:WSON-8-1EP_2x2mm_P0.5mm_HAND1, B.Cu at (80.6, 117.1)
- added U7: DRV8837DSGR, malenki-nano:WSON-8-1EP_2x2mm_P0.5mm_HAND1, B.Cu at (58.6, 117.1)
- added U7: DRV8837DSGR, malenki-nano:WSON-8-1EP_2x2mm_P0.5mm_HAND1, B.Cu at (36.6, 90.1)
- added U7: DRV8837DSGR, malenki-nano:WSON-8-1EP_2x2mm_P0.5mm_HAND1, B.Cu at (102.6, 63.1)
- added U7: DRV8837DSGR, malenki-nano:WSON-8-1EP_2x2mm_P0.5mm_HAND1, B.Cu at (36.6, 63.1)
- added U7: DRV8837DSGR, malenki-nano:WSON-8-1EP_2x2mm_P0.5mm_HAND1, B.Cu at (80.6, 90.1)
- added U7: DRV8837DSGR, malenki-nano:WSON-8-1EP_2x2mm_P0.5mm_HAND1, B.Cu at (102.6, 117.1)
- added U7: DRV8837DSGR, malenki-nano:WSON-8-1EP_2x2mm_P0.5mm_HAND1, B.Cu at (58.6, 63.1)
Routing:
- net VSENSE: track 131.4 -> 230.4 mm, vias 0 -> 24
- net VLOGIC: track 568.0 -> 597.6 mm
- net UPDI: track 392.8 -> 410.4 mm
- net GND: track 1409.9 -> 1395.7 mm, vias 60 -> 72
- net MOTOR1F: track 261.1 -> 270.0 mm
- net unconnected-(J2-Pad7): track 0.00 -> 4.20 mm
- net unconnected-(J2-Pad2): track 0.00 -> 4.20 mm
- net Net-(J2-Pad7): track 4.20 -> 0.00 mm
- net Net-(J2-Pad2): track 4.20 -> 0.00 mm
- net SPI_SCK: track 91.4 -> 90.6 mm
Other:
- outline, holes or cut-outs redrawn
- board text added: "@markxr 2021.B"
- board text added: "Malenki-Nano Panel12 - tiny817 - 19.6.2021"
- board text removed: "@markxr 2021"
- board text removed: "Malenki-Nano Panel 12 21.2.2021"
